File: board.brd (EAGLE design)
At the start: 51.7 x 80 mm, 17 parts

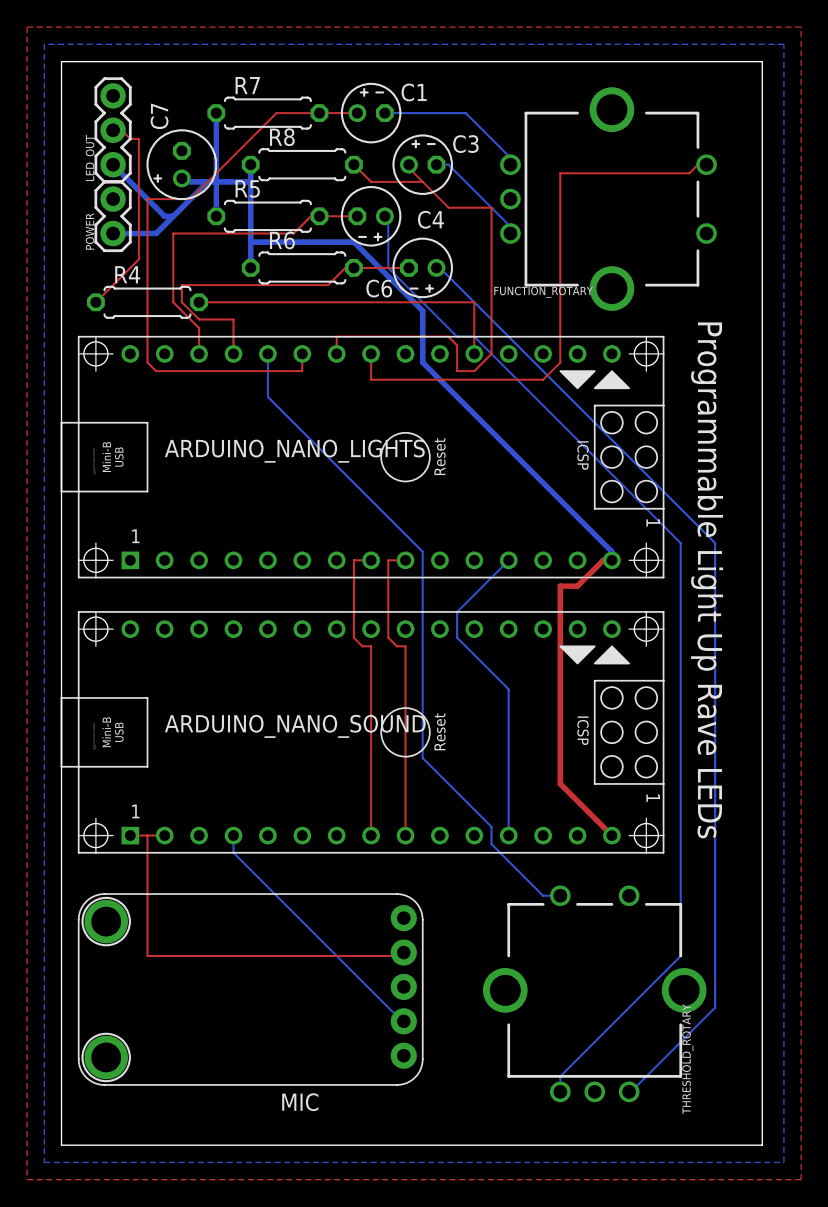
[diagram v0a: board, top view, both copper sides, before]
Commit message: fixing mistakes from prototype
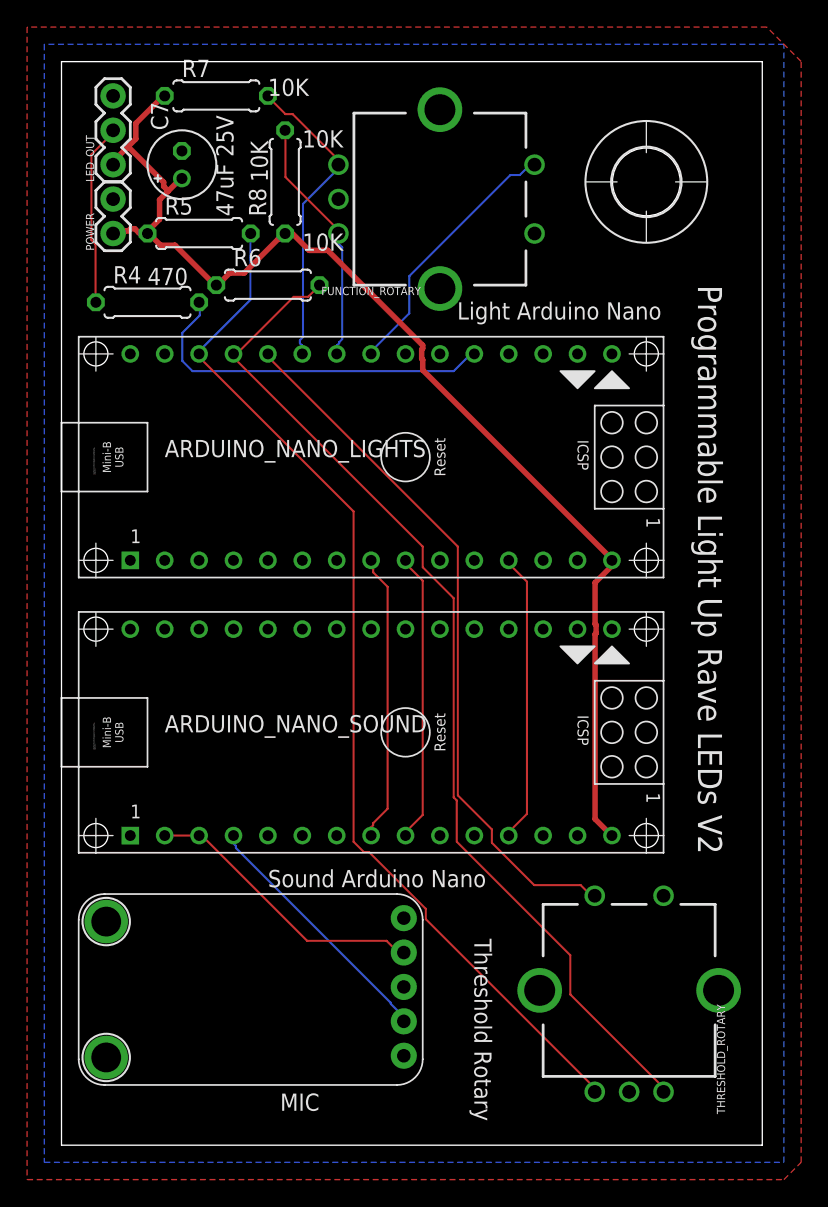
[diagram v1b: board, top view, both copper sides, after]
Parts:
- removed C1, C3, C4, C6: 0.1uF, 25V, rcl:E2-4
- added U$2: (no value), holes:5,0
- moved FUNCTION_ROTARY 12.7 mm to (27.9, 69.8)
- moved R5 5.24 mm to (10.2, 67.3)
- moved R7 4.02 mm to (11.4, 77.5)
- moved R6 2.84 mm to (15.2, 63.5)
- moved THRESHOLD_ROTARY 2.54 mm to (41.9, 11.4)
- moved R8 1.80 mm to (16.5, 71.1), turned to 90 degrees
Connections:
- removed net N$16: C6.+, THRESHOLD_ROTARY.B
- removed net N$4: ARDUINO_NANO_LIGHTS.25, C1.+, R7.2
- removed net N$6: ARDUINO_NANO_LIGHTS.24, C3.+, R8.2
- removed net N$7: ARDUINO_NANO_LIGHTS.28, C4.-, R5.2
- net MIC_VCC: now also ARDUINO_NANO_SOUND.3; no longer ARDUINO_NANO_SOUND.1
- net N$13: now also ARDUINO_NANO_LIGHTS.25, R7.2; no longer C1.-
- net N$14: now also ARDUINO_NANO_LIGHTS.24, R8.2; no longer C3.-
- net N$15: now also ARDUINO_NANO_LIGHTS.28, R5.2; no longer C4.+
- net N$2: now also THRESHOLD_ROTARY.B; no longer C6.-
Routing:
- net N$16: track 72.4 -> 0.00 mm
- net N$2: track 25.4 -> 76.3 mm
- net N$4: track 43.2 -> 0.00 mm
- net N$6: track 39.7 -> 0.00 mm
- net N$7: track 23.8 -> 0.00 mm
- net N$3: track 41.4 -> 19.6 mm
- net N$13: track 11.9 -> 22.8 mm
- net N$14: track 8.58 -> 18.4 mm
- net +5V: track 98.8 -> 89.3 mm
- net MIC_VCC: track 30.4 -> 21.2 mm
- net LED_OUT: track 24.1 -> 27.3 mm
- net N$1: track 49.7 -> 52.2 mm
- net N$20: track 15.5 -> 13.5 mm
- net 5V: track 23.5 -> 21.5 mm
- net N$18: track 22.5 -> 21.3 mm
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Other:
- board text added: "10K"
- board text added: "470"
- board text added: "47uF 25V"
- board text added: "Light Arduino Nano"
- board text added: "Programmable Light Up Rave LEDs V2"
- board text added: "Sound Arduino Nano"
- board text added: "Threshold Rotary"
- board text removed: "Programmable Light Up Rave LEDs"
